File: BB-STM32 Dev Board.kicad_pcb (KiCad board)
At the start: 2 copper layers, 48 x 51 mm, 57 parts, among them IC1 FT260Q, IC2 TPS63070RNMR, J1 216990-0003, J2 SPI, J3 USART, J5 I2C, J6 3V-16V, J7 BATTERY, SW1 BOOT, SW2 RESET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

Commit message: First Run of board.
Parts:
- removed C10: 10uF, Capacitor_SMD:C_0402_1005Metric_Pad0.74x0.62mm_HandSolder
- removed C11: 47uF, Capacitor_SMD:C_0402_1005Metric_Pad0.74x0.62mm_HandSolder
- removed C9: 100nF, Capacitor_SMD:C_0402_1005Metric_Pad0.74x0.62mm_HandSolder
- removed IC2: TPS63070RNMR, Converter_DCDC_Custom:TPS630701RNMR
- removed M1: ~, Wireless_Custom:BB-STM32WL
- removed R13: 470K, Resistor_SMD:R_0402_1005Metric_Pad0.72x0.64mm_HandSolder
- removed R14: 150K, Resistor_SMD:R_0402_1005Metric_Pad0.72x0.64mm_HandSolder
- added D7: ~, Diode_SMD:D_SOD-123, F.Cu at (140.5, 100.1)
- added D8: ~, Diode_SMD:D_SOD-123, F.Cu at (128.5, 83.5)
- added J8: Conn_01x12, Connector_PinSocket_2.54mm:PinSocket_1x12_P2.54mm_Vertical, F.Cu at (150.7, 83.6)
- added J9: Conn_01x12, Connector_PinSocket_2.54mm:PinSocket_1x12_P2.54mm_Vertical, F.Cu at (125.3, 83.6)
- added R20: 50K, Resistor_SMD:R_0402_1005Metric_Pad0.72x0.64mm_HandSolder, F.Cu at (148.0, 96.2)
- added R21: 97K, Resistor_SMD:R_0402_1005Metric_Pad0.72x0.64mm_HandSolder, F.Cu at (148.0, 98.8)
- added SW4: ON_OFF, Button_Switch_THT:SW_Slide_SPDT_Angled_CK_OS102011MA1Q, F.Cu at (150.5, 75.2)
- added U2: TLV62569PDDCR, Component Libraries:SOT95P280X110-6N, F.Cu at (142.2, 85.0)
- C12, C13, C8: footprint Capacitor_SMD:C_0402_1005Metric_Pad0.74x0.62mm_HandSolder -> Capacitor_SMD:C_0805_2012Metric_Pad1.18x1.45mm_HandSolder
- C7: value 22uF -> 4.7uF
- D4: footprint Diode_SMD:D_SOD-323_HandSoldering -> Diode_SMD:D_SOD-123
- IC1: footprint FT260Q:QFN50P500X500X80-29N-D -> Component Libraries:QFN50P500X500X80-29N-D
- J1: footprint 216990-0003:2169900003 -> Component Libraries:2169900003
- L1: value 2.2uH -> 1uH; footprint Inductor_SMD:L_0805_2012Metric_Pad1.15x1.40mm_HandSolder -> Component Libraries:Bourns SRP4020TA
- R1, R2, R3: moved to F.Cu
- R10, R16, R17, R9: value ???? -> 665
- R11: value 10K -> 453K
- moved R12 6.88 mm to (145.0, 84.8), turned to 90 degrees
- moved J7 6.25 mm to (137.8, 75.5)
- moved L1 5.51 mm to (141.5, 89.5), turned to 0 degrees
- moved C7 5.24 mm to (139.2, 85.2), turned to -90 degrees
- moved R2 4.53 mm to (140.5, 113.0), turned to 90 degrees
- moved J6 4.00 mm to (128.0, 75.5)
- moved R3 3.91 mm to (140.5, 105.0), turned to -90 degrees
- moved R1 3.78 mm to (135.8, 113.8)
- moved R11 3.61 mm to (146.0, 84.8)
- moved D4 3.06 mm to (134.8, 82.0)
- moved C8 2.49 mm to (145.8, 88.2), turned to -90 degrees
- moved C13 1.03 mm to (135.5, 87.0)
- moved R6 0.71 mm to (138.5, 103.8)
- moved R7 0.71 mm to (137.5, 103.8)
- moved R8 0.71 mm to (136.5, 103.8)
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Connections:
- C12 pad 1: VBAT -> Net-(D8-A)
- C8 pad 1: VBAT -> +3V3
- J7 pad 1: VBAT -> Net-(D8-K)
- L1 pad 2: Net-(IC2-L2) -> +3V3
- R11 pad 1: VBAT -> Net-(U2-FB)
- R11 pad 2: Net-(IC2-EN) -> +3V3
- R12 pad 1: +3V3 -> GND
- R12 pad 2: Net-(IC2-PG) -> Net-(U2-FB)
- R16 pad 2: VBAT -> Net-(D8-A)
- U1 pad 3: VBAT -> Net-(D8-A)
- U1 pad 4: VBAT -> Net-(D8-A)
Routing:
- net VBAT: track 0.00 -> 38.2 mm
- net Net-(D4-K): track 0.00 -> 28.5 mm
- net USB_VBUS: track 0.00 -> 26.4 mm, vias 0 -> 2
- net Net-(D8-K): track 0.00 -> 24.9 mm, vias 0 -> 2
- net Net-(J8-Pin_5): track 0.00 -> 9.36 mm
- net +3V3: track 62.7 -> 70.5 mm, vias 3 -> 1
- net /USB_DP: track 0.00 -> 4.81 mm
- net Net-(U2-SW): track 0.00 -> 4.11 mm
- net /USB_DN: track 0.00 -> 4.00 mm
- net Net-(JP1-A): track 0.00 -> 3.39 mm
- net Net-(IC2-FB): track 3.02 -> 0.00 mm
- net Net-(D5-K): track 0.00 -> 3.00 mm
- net Net-(IC2-EN): track 2.97 -> 0.00 mm
- net Net-(IC2-PG): track 2.75 -> 0.00 mm
- net Net-(U2-FB): track 0.00 -> 2.73 mm
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- added copper zone on F.Cu, net Net-(D4-K)
- added copper zone on F.Cu, net Net-(D8-A)
- removed copper zone on F.Cu, net +3V3
- removed copper zone on F.Cu, net Net-(IC2-L2)
- removed copper zone on F.Cu, net Net-(U2-SW)
- removed copper zone on F.Cu, net VBAT
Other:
- board text added: "OFF"
- board text added: "ON"
- board text added: "U.FL"

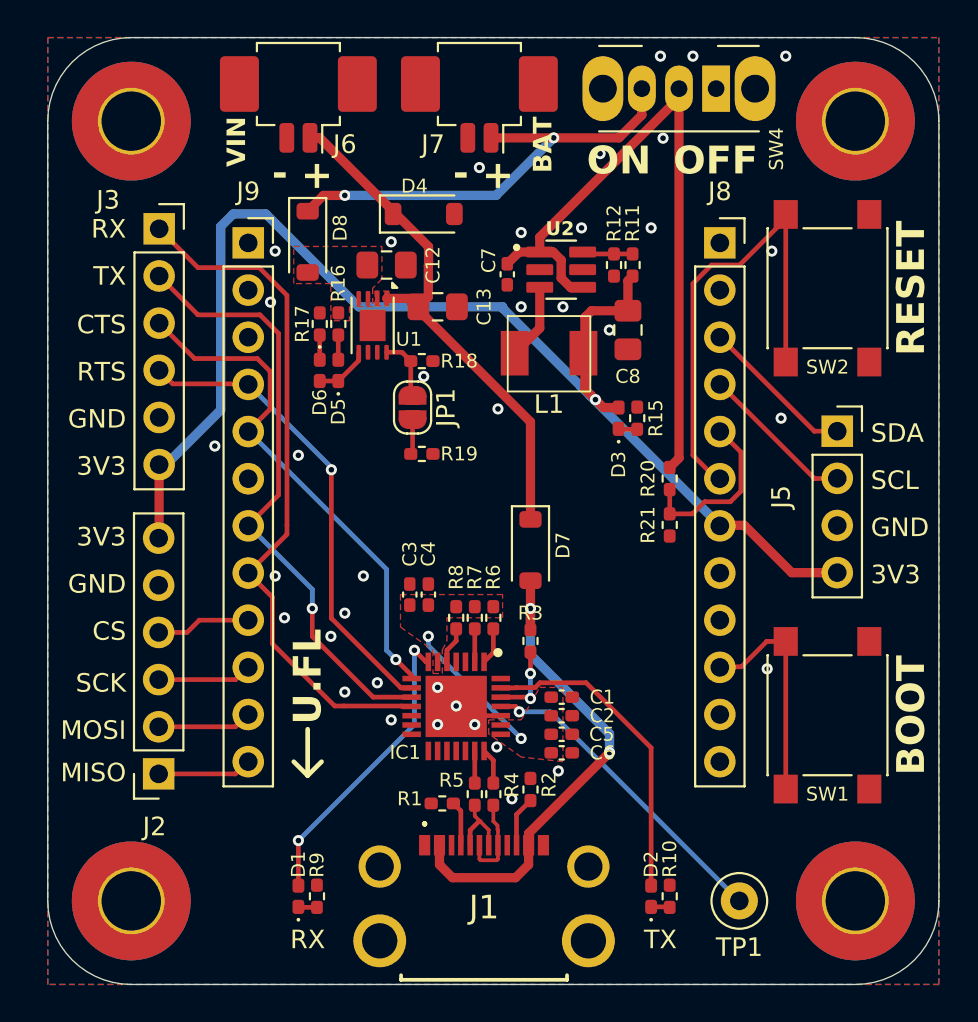
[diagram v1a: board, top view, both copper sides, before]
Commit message: Added Images and fixed USB Virtual COM Port.
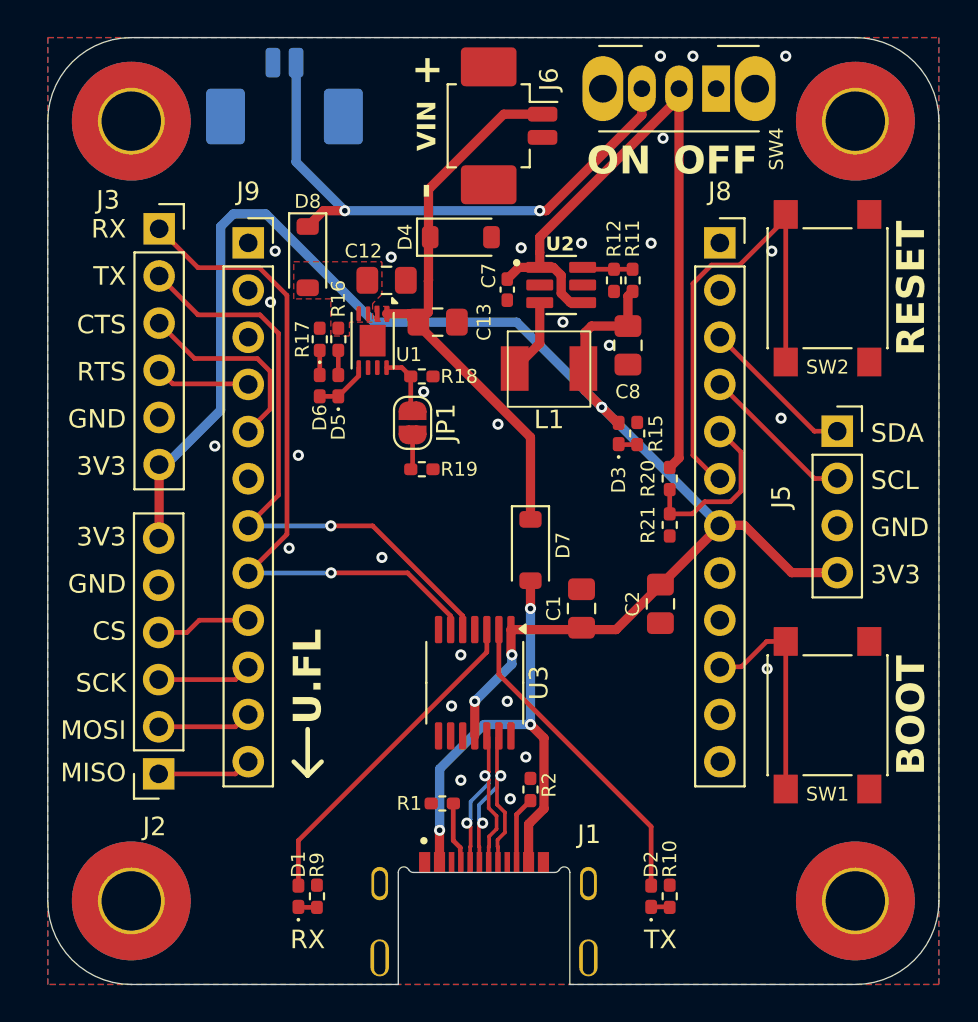
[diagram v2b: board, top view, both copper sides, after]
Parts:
- removed C3, C5: 4.7uF, Capacitor_SMD:C_0402_1005Metric_Pad0.74x0.62mm_HandSolder
- removed C4, C6: 0.1uF, Capacitor_SMD:C_0402_1005Metric_Pad0.74x0.62mm_HandSolder
- removed IC1: FT260Q, Component Libraries:QFN50P500X500X80-29N-D
- removed R3: 5k1, Resistor_SMD:R_0402_1005Metric_Pad0.72x0.64mm_HandSolder
- removed R4, R5: 33, Resistor_SMD:R_0402_1005Metric_Pad0.72x0.64mm_HandSolder
- removed R6, R7, R8: 10K, Resistor_SMD:R_0402_1005Metric_Pad0.72x0.64mm_HandSolder
- removed TP1: TestPoint, TestPoint:TestPoint_Loop_D1.80mm_Drill1.0mm_Beaded
- added U3: MCP2221AxST, Package_SO:TSSOP-14_4.4x5mm_P0.65mm, F.Cu at (137.5, 107.2)
- C1: value 4.7uF -> 10uF; footprint Capacitor_SMD:C_0402_1005Metric_Pad0.74x0.62mm_HandSolder -> Capacitor_SMD:C_0805_2012Metric_Pad1.18x1.45mm_HandSolder
- C2: value 0.1uF -> 10uF; footprint Capacitor_SMD:C_0402_1005Metric_Pad0.74x0.62mm_HandSolder -> Capacitor_SMD:C_0805_2012Metric_Pad1.18x1.45mm_HandSolder
- J1: value 216990-0003 -> 2169900003; footprint Component Libraries:2169900003 -> Downloaded Footprints:MOLEX_2169900003
- J7: moved to B.Cu
- moved J6 10.9 mm to (138.8, 77.2), turned to -90 degrees
- moved J7 10.5 mm to (127.2, 76.2)
- moved C2 8.04 mm to (147.5, 103.0), turned to -90 degrees
- moved C1 4.89 mm to (143.2, 103.2), turned to 90 degrees
- moved D4 2.36 mm to (136.8, 83.2)
- moved J1 2.07 mm to (138.0, 122.1)
- moved C12 0.83 mm to (132.8, 85.6)
- moved C13 0.83 mm to (135.5, 87.8)
- moved C7 0.83 mm to (139.2, 86.1)
- moved C8 0.83 mm to (145.8, 89.1)
- moved D3 0.83 mm to (145.2, 93.8)
- moved D5 0.83 mm to (130.2, 91.2)
- moved D6 0.83 mm to (129.2, 91.2)
- moved D8 0.83 mm to (128.5, 84.3)
- moved JP1 0.83 mm to (134.2, 93.2)
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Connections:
- net /USB_CTS renamed Net-(J3-Pin_4)
- net /USB_RTS renamed Net-(J3-Pin_3)
- C1 pad 1: /VCCIN -> +3V3
- C2 pad 1: /VCCIN -> +3V3
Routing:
- net Net-(J3-Pin_4): track 25.4 -> 5.10 mm, vias 1 -> 0
- net +3V3: track 70.5 -> 89.6 mm, vias 1 -> 3
- net Net-(IC1-FSOURCE): track 17.2 -> 0.00 mm, vias 1 -> 0
- net Net-(J3-Pin_3): track 27.7 -> 10.8 mm, vias 1 -> 0
- net /USB_DN: track 4.00 -> 12.5 mm, vias 0 -> 2
- net /USB_DP: track 4.81 -> 12.5 mm, vias 0 -> 2
- net /VCCIN: track 7.57 -> 0.00 mm, vias 2 -> 0
- net Net-(D8-K): track 24.9 -> 31.0 mm
- net Net-(IC1-VBUS_DET): track 4.13 -> 0.00 mm, vias 2 -> 0
- net GND: track 2.61 -> 0.00 mm, vias 37 -> 27
- net Net-(D4-K): track 28.5 -> 30.6 mm
- net Net-(IC1-DP): track 2.07 -> 0.00 mm
- net Net-(IC1-DEBUGGER): track 1.98 -> 0.00 mm
- net Net-(IC1-DCNF1): track 1.98 -> 0.00 mm
- net Net-(IC1-STEST_RSTN): track 1.78 -> 0.00 mm
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- removed copper zone on F.Cu, net /VCCIN
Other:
- outline, holes or cut-outs redrawn
- board text added: "BB-STM32WL Dev Board V2.0"
